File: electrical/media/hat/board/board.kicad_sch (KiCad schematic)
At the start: 9 parts, among them J101 RPI_PINS, J102 5V_IN, SW101 TS50810-411-02528

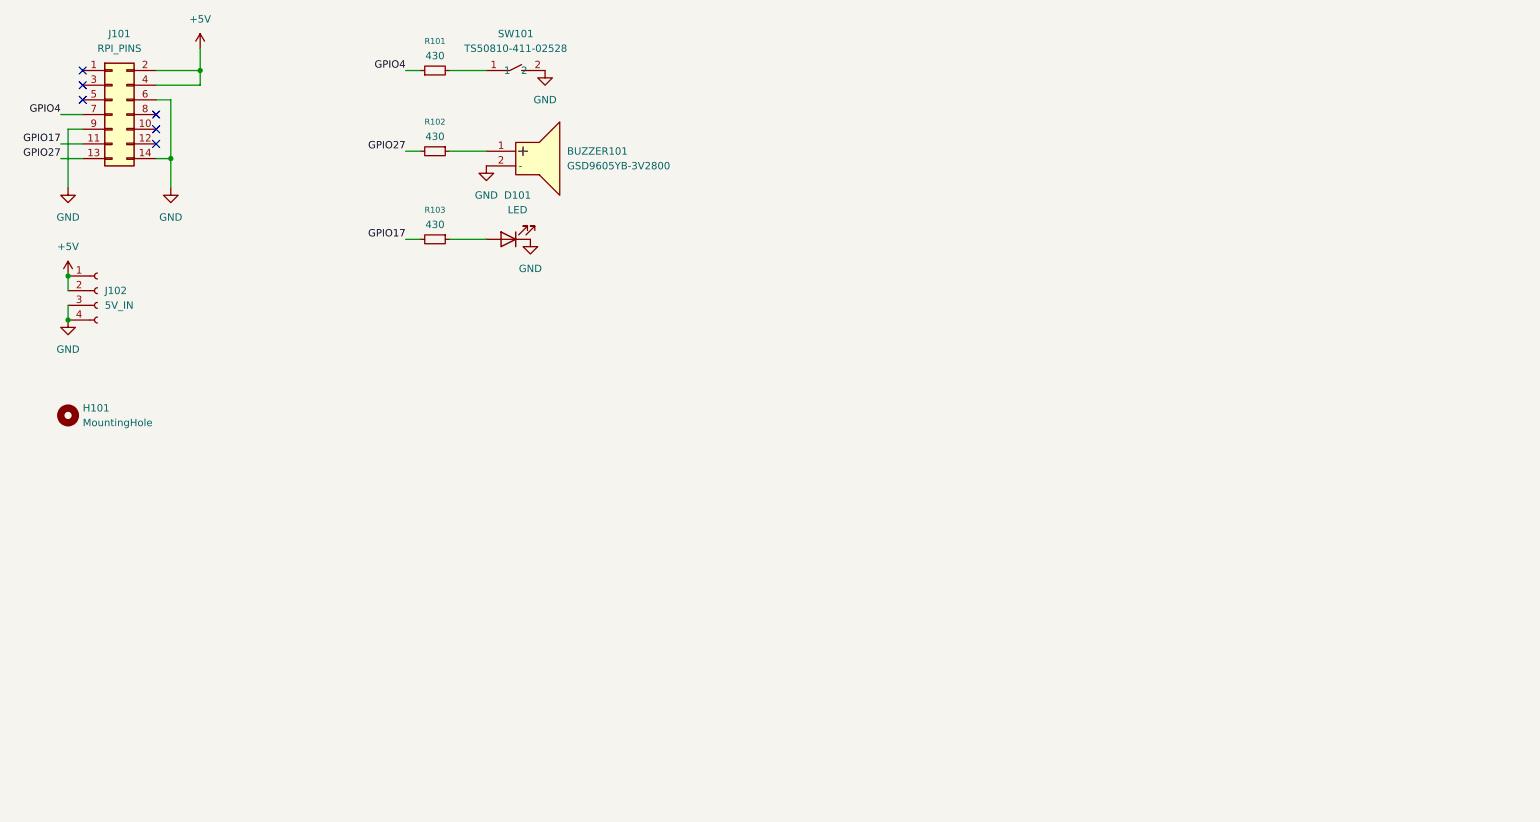
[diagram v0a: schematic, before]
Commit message: media hat power fix fabrication ready
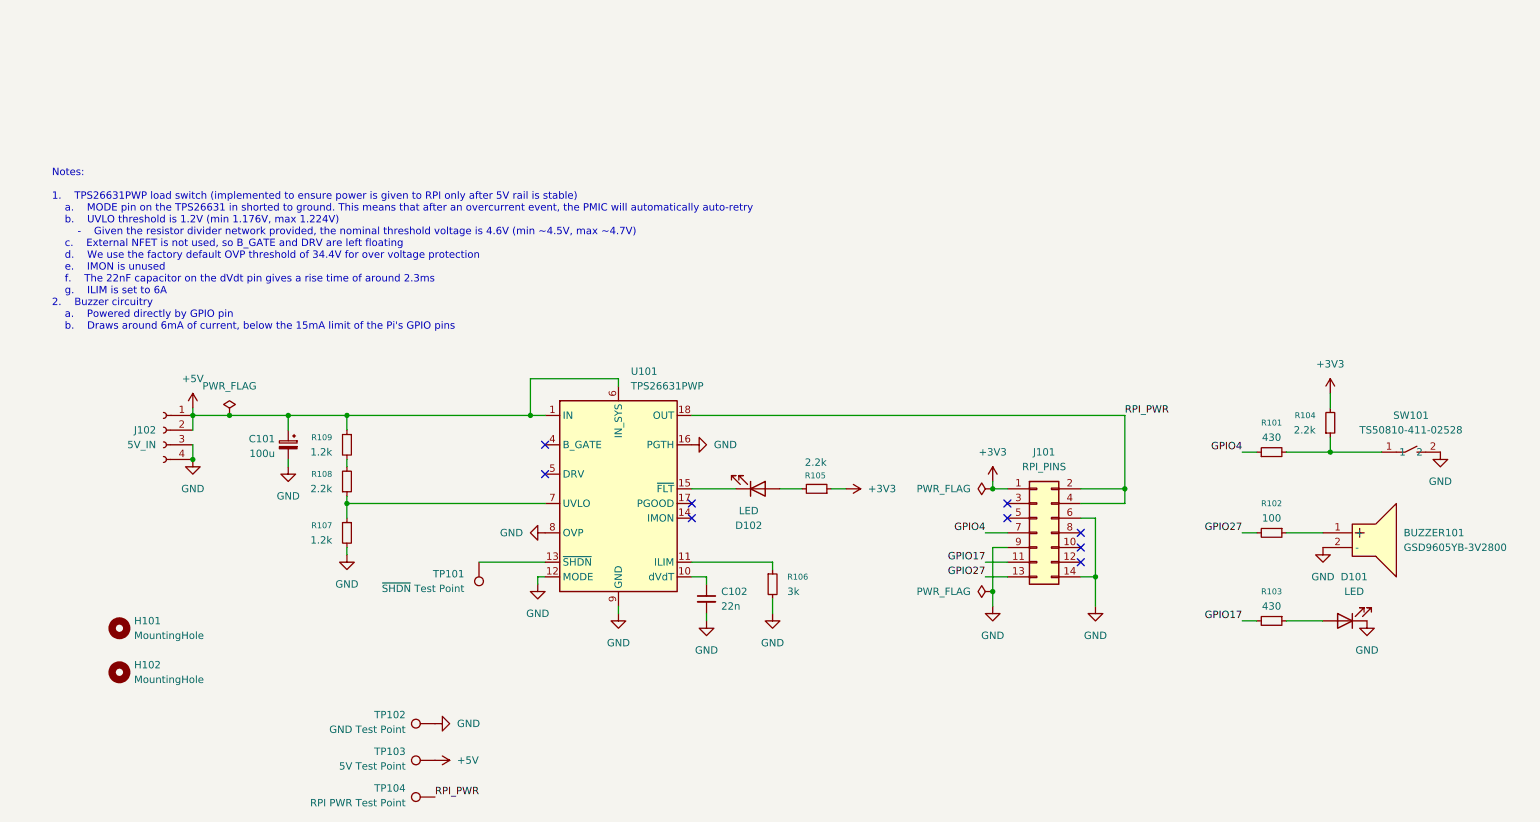
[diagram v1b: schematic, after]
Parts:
- added C101: 100u, Capacitor_Tantalum_SMD:CP_EIA-7343-31_Kemet-D, symbol Device:C_Polarized_Small
- added C102: 22n, Capacitor_SMD:C_0402_1005Metric, symbol Device:C_Small
- added D102: LED, LED_SMD:LED_0603_1608Metric, symbol Device:LED
- added H102: MountingHole, MountingHole:MountingHole_2.5mm, symbol Mechanical:MountingHole
- added R104, R105, R108: 2.2k, Resistor_SMD:R_0402_1005Metric, symbol Device:R_Small
- added R106: 3k, Resistor_SMD:R_0603_1608Metric, symbol Device:R_Small
- added R107, R109: 1.2k, Resistor_SMD:R_0402_1005Metric, symbol Device:R_Small
- added TP101: ~{SHDN} Test Point, TestPoint:TestPoint_Keystone_5015_Micro_Mini, symbol Connector:TestPoint
- added TP102: GND Test Point, TestPoint:TestPoint_Keystone_5015_Micro_Mini, symbol Connector:TestPoint
- added TP103: 5V Test Point, TestPoint:TestPoint_Keystone_5015_Micro_Mini, symbol Connector:TestPoint
- added TP104: RPI PWR Test Point, TestPoint:TestPoint_Keystone_5015_Micro_Mini, symbol Connector:TestPoint
- added U101: TPS26631PWP, Package_SO:HTSSOP-20-1EP_4.4x6.5mm_P0.65mm_EP3.4x6.5mm_Mask2.96x2.96mm_ThermalVias, symbol Power_Management:TPS26631PWP
- H101: footprint MountingHole:MountingHole_3.2mm_M3 -> MountingHole:MountingHole_2.5mm
- R102: value 430 -> 100; LCSC C137868 -> C25076
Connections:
- net +5V: now also C101.1, R109.1, TP103.1, U101.1 (IN), U101.2 (IN), U101.3 (IN), U101.6 (IN_SYS); no longer J101.2 (Pin_2), J101.4 (Pin_4)
- net GND: now also C101.2, C102.2, R106.2, R107.2, TP102.1, U101.12 (MODE), U101.16 (PGTH), U101.21 (GND), U101.8 (OVP), U101.9 (GND)
- net at R101.2, SW101.1: now also R104.1
- net +3V3: now reaches J101.1 (Pin_1)
- net +3V3: now also R104.2, R105.1
- new net: R107.1, R108.1, U101.7 (UVLO)
- new net: R108.2, R109.2
- new net: C102.1, U101.10 (dVdT)
- new net: TP101.1, U101.13 (~{SHDN})
- new net: D102.1 (K), U101.15 (~{FLT})
- new net: D102.2 (A), R105.2
- new net: R106.1, U101.11 (ILIM)
- new net RPI_PWR: J101.2 (Pin_2), J101.4 (Pin_4), TP104.1, U101.18 (OUT), U101.19 (OUT), U101.20 (OUT)
- no-connect marks 6 -> 9
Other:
- note added: "Notes: 1. TPS26631PWP load switch (implemented to ensure power is given to RPI only after 5V rail is stable) a. MODE pin on the TPS26631 in shorted to ground. This means that after an overcurrent event, the PMIC will automatically auto-retry b. UVLO threshold is 1.2V (min 1.176V, max 1.224V) - Given the resistor divider network provided, the nominal threshold voltage is 4.6V (min ~4.5V, max ~4.7V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"
- moved on the sheet: BUZZER101, D101, H101, J101, J102, R101, R102, R103, SW101

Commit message: flip connector polarity
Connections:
- net +5V: now also J102.3 (Pin_3), J102.4 (Pin_4); no longer J102.1 (Pin_1), J102.2 (Pin_2)
- net GND: now also J102.1 (Pin_1), J102.2 (Pin_2); no longer J102.3 (Pin_3), J102.4 (Pin_4)
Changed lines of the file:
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@@
 	)
 	(junction
+		(at 44.45 93.98)
+		(diameter 0)
+		(color 0 0 0 0)
+	)
+	(junction
 		(at 182.88 116.84)
 		(diameter 0)
@@
 	)
 	(junction
-		(at 44.45 93.98)
-		(diameter 0)
-		(color 0 0 0 0)
-	)
-	(junction
 		(at 102.87 86.36)
 		(diameter 0)
@@
 	)
 	(symbol
-		(lib_id "Connector:Conn_01x04_Socket")
-		(at 39.37 88.9 0)
-		(mirror y)
-		(unit 1)
-		(body_style 1)
-		(exclude_from_sim no)
-		(in_bom yes)
-		(on_board yes)
-		(in_pos_files yes)
-		(dnp no)
-		(fields_autoplaced yes)
-		(property "Reference" "J102"
-			(at 38.1 88.8999 0)
-			(show_name no)
-			(do_not_autoplace no)
-			(effects
-				(font
-					(size 1.27 1.27)
-				)
-				(justify left)
-			)
-		)
-		(property "Value" "5V_IN"
-			(at 38.1 91.4399 0)
-			(show_name no)
-			(do_not_autoplace no)
-			(effects
-				(font
-					(size 1.27 1.27)
-				)
-				(justify left)
-			)
-		)
-		(property "Footprint" "Connector_JST:JST_XH_B4B-XH-A_1x04_P2.50mm_Vertical"
-			(at 39.37 88.9 0)
-			(hide yes)
-			(show_name no)
-			(do_not_autoplace no)
-			(effects
-				(font
-					(size 1.27 1.27)
-				)
-			)
-		)
-		(property "Datasheet" ""
-			(at 39.37 88.9 0)
-			(hide yes)
-			(show_name no)
-			(do_not_autoplace no)
-			(effects
-				(font
-					(size 1.27 1.27)
-				)
-			)
-		)
-		(property "Description" "Generic connector, single row, 01x04, script generated"
-			(at 39.37 88.9 0)
-			(hide yes)
-			(show_name no)
-			(do_not_autoplace no)
-			(effects
-				(font
-					(size 1.27 1.27)
-				)
-			)
-		)
-		(property "LCSC" "C144395"
-			(at 39.37 88.9 0)
-			(hide yes)
-			(show_name no)
-			(do_not_autoplace no)
-			(effects
-				(font
-					(size 1.27 1.27)
-				)
-			)
-		)
-		(pin "3"
-		)
-		(pin "4"
-		)
-		(pin "2"
-		)
-		(pin "1"
-		)
-		(instances
-			(project "board"
-				(path "/29e64e60-14ac-49fa-a4d0-21e58b105b3c"
-					(reference "J102")
-					(unit 1)
-				)
-			)
-		)
-	)
-	(symbol
 		(lib_id "Mechanical:MountingHole")
 		(at 31.75 123.19 0)
@@
 					(unit 1)
 				)
+			)
+		)
+	)
+	(symbol
+		(lib_id "Connector:Conn_01x04_Socket")
+		(at 39.37 91.44 180)
+		(unit 1)
+		(body_style 1)
+		(exclude_from_sim no)
+		(in_bom yes)
+		(on_board yes)
+		(in_pos_files yes)
+		(dnp no)
+		(property "Reference" "J102"
+			(at 38.1 91.4401 0)
+			(show_name no)
+			(do_not_autoplace no)
+			(effects
+				(font
+					(size 1.27 1.27)
+				)
+				(justify left)
+			)
+		)
+		(property "Value" "5V_IN"
+			(at 38.1 88.9001 0)
+			(show_name no)
+			(do_not_autoplace no)
+			(effects
+				(font
+					(size 1.27 1.27)
+				)
+				(justify left)
+			)
+		)
+		(property "Footprint" "Connector_JST:JST_XH_B4B-XH-A_1x04_P2.50mm_Vertical"
+			(at 39.37 91.44 0)
+			(hide yes)
+			(show_name no)
+			(do_not_autoplace no)
+			(effects
+				(font
+					(size 1.27 1.27)
+				)
+			)
+		)
+		(property "Datasheet" ""
+			(at 39.37 91.44 0)
+			(hide yes)
+			(show_name no)
+			(do_not_autoplace no)
+			(effects
+				(font
+					(size 1.27 1.27)
+				)
+			)
+		)
+		(property "Description" "Generic connector, single row, 01x04, script generated"
+			(at 39.37 91.44 0)
+			(hide yes)
+			(show_name no)
+			(do_not_autoplace no)
+			(effects
+				(font
+					(size 1.27 1.27)
+				)
+			)
+		)
+		(property "LCSC" "C144395"
+			(at 39.37 91.44 0)
+			(hide yes)
+			(show_name no)
+			(do_not_autoplace no)
+			(effects
+				(font
+					(size 1.27 1.27)
+				)
+			)
+		)
+		(pin "3"
+		)
+		(pin "4"
+		)
+		(pin "2"
+		)
+		(pin "1"
+		)
+		(instances
+			(project "board"
+				(path "/29e64e60-14ac-49fa-a4d0-21e58b105b3c"
+					(reference "J102")
+					(unit 1)
+				)

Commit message: change FLT to RED LED
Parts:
- D101: value LED -> Green LED
- D102: value LED -> Red LED; LCSC C965804 -> C2286
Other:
- moved on the sheet: D101
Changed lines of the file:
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@@
 	(wire
 		(pts
+			(xy 247.65 121.92) (xy 252.73 121.92)
+		)
+		(stroke
+			(width 0)
+			(type default)
+		)
+	)
+	(wire
+		(pts
 			(xy 93.98 111.76) (xy 105.41 111.76)
 		)
@@
 	(symbol
 		(lib_id "power:GND")
+		(at 252.73 121.92 90)
+		(unit 1)
+		(body_style 1)
+		(exclude_from_sim no)
+		(in_bom yes)
+		(on_board yes)
+		(in_pos_files yes)
+		(dnp no)
+		(fields_autoplaced yes)
+		(property "Reference" "#PWR0107"
+			(at 259.08 121.92 0)
+			(hide yes)
+			(show_name no)
+			(do_not_autoplace no)
+			(effects
+				(font
+					(size 1.27 1.27)
+				)
+			)
+		)
+		(property "Value" "GND"
+			(at 256.54 121.9199 90)
+			(show_name no)
+			(do_not_autoplace no)
+			(effects
+				(font
+					(size 1.27 1.27)
+				)
+				(justify right)
+			)
+		)
+		(property "Footprint" ""
+			(at 252.73 121.92 0)
+			(hide yes)
+			(show_name no)
+			(do_not_autoplace no)
+			(effects
+				(font
+					(size 1.27 1.27)
+				)
+			)
+		)
+		(property "Datasheet" ""
+			(at 252.73 121.92 0)
+			(hide yes)
+			(show_name no)
+			(do_not_autoplace no)
+			(effects
+				(font
+					(size 1.27 1.27)
+				)
+			)
+		)
+		(property "Description" "Power symbol creates a global label with name \"GND\" , ground"
+			(at 252.73 121.92 0)
+			(hide yes)
+			(show_name no)
+			(do_not_autoplace no)
+			(effects
+				(font
+					(size 1.27 1.27)
+				)
+			)
+		)
+		(pin "1"
+		)
+		(instances
+			(project "board"
+				(path "/29e64e60-14ac-49fa-a4d0-21e58b105b3c"
+					(reference "#PWR0107")
+					(unit 1)
+				)
+			)
+		)
+	)
+	(symbol
+		(lib_id "power:GND")
 		(at 240.03 109.22 0)
 		(unit 1)
@@
 			)
 		)
-		(property "Value" "LED"
+		(property "Value" "Red LED"
 			(at 140.6525 102.87 0)
 			(show_name no)
@@
 			)
 		)
-		(property "LCSC" "C965804"
+		(property "LCSC" "C2286"
 			(at 142.24 99.06 0)
 			(hide yes)
@@
 	)
 	(symbol
-		(lib_id "power:GND")
-		(at 247.65 121.92 0)
-		(unit 1)
-		(body_style 1)
-		(exclude_from_sim no)
-		(in_bom yes)
-		(on_board yes)
-		(in_pos_files yes)
-		(dnp no)
-		(fields_autoplaced yes)
-		(property "Reference" "#PWR0107"
-			(at 247.65 128.27 0)
-			(hide yes)
-			(show_name no)
-			(do_not_autoplace no)
-			(effects
-				(font
-					(size 1.27 1.27)
-				)
-			)
-		)
-		(property "Value" "GND"
-			(at 247.65 127 0)
-			(show_name no)
-			(do_not_autoplace no)
-			(effects
-				(font
-					(size 1.27 1.27)
-				)
-			)
-		)
-		(property "Footprint" ""
-			(at 247.65 121.92 0)
-			(hide yes)
-			(show_name no)
-			(do_not_autoplace no)
-			(effects
-				(font
-					(size 1.27 1.27)
-				)
-			)
-		)
-		(property "Datasheet" ""
-			(at 247.65 121.92 0)
-			(hide yes)
-			(show_name no)
-			(do_not_autoplace no)
-			(effects
-				(font
-					(size 1.27 1.27)
-				)
-			)
-		)
-		(property "Description" "Power symbol creates a global label with name \"GND\" , ground"
-			(at 247.65 121.92 0)
-			(hide yes)
-			(show_name no)
-			(do_not_autoplace no)
-			(effects
-				(font
-					(size 1.27 1.27)
-				)
-			)
-		)
-		(pin "1"
-		)
-		(instances
-			(project "board"
-				(path "/29e64e60-14ac-49fa-a4d0-21e58b105b3c"
-					(reference "#PWR0107")
-					(unit 1)
-				)
-			)
-		)
-	)
-	(symbol
 		(lib_id "Device:R_Small")
 		(at 71.12 91.44 0)
@@
 	(symbol
 		(lib_id "Device:LED")
-		(at 243.84 121.92 180)
+		(at 243.84 121.92 0)
+		(mirror y)
 		(unit 1)
 		(body_style 1)
@@
 		(in_pos_files yes)
 		(dnp no)
-		(fields_autoplaced yes)
 		(property "Reference" "D101"
-			(at 245.4275 114.3 0)
+			(at 245.4275 129.54 0)
 			(show_name no)
 			(do_not_autoplace no)
@@
 			)
 		)
-		(property "Value" "LED"
-			(at 245.4275 116.84 0)
+		(property "Value" "Green LED"
+			(at 245.4275 127 0)
 			(show_name no)
 			(do_not_autoplace no)
